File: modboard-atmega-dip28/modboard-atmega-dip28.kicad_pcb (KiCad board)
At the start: 2 copper layers, 57.5 x 52.6 mm, 10 parts, among them J1 modboard-edge-connector, J2 Conn_01x03_Male, U1 ATMEGA328P-PU, Y1 Crystal

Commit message: Added logo
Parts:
- added ATmega-DIP28: LOGO_BRD_REF, qboards_aesthetics:logo_url-3mm, B.Cu at (126.6, 71.3)
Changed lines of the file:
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@@
     (tracks 381)
     (zones 0)
-    (modules 10)
+    (modules 11)
     (nets 28)
   )
   (page A4)
   (layers
-    (0 F.Cu signal)
-    (31 B.Cu signal)
+    (0 F.Cu signal hide)
+    (31 B.Cu signal hide)
     (32 B.Adhes user hide)
     (33 F.Adhes user hide)
@@
   )
   (setup
-    (last_trace_width 0.61)
+    (last_trace_width 0.3048)
     (user_trace_width 0.61)
     (trace_clearance 0.2)
@@
     (add_net "Net-(C2-Pad1)")
     (add_net "Net-(C3-Pad1)")
-    (add_net "Net-(J1-Pad10)")
-    (add_net "Net-(J1-Pad11)")
-    (add_net "Net-(J1-Pad12)")
-    (add_net "Net-(J1-Pad13)")
-    (add_net "Net-(J1-Pad14)")
-    (add_net "Net-(J1-Pad15)")
-    (add_net "Net-(J1-Pad16)")
-    (add_net "Net-(J1-Pad17)")
-    (add_net "Net-(J1-Pad19)")
-    (add_net "Net-(J1-Pad21)")
-    (add_net "Net-(J1-Pad22)")
-    (add_net "Net-(J1-Pad23)")
-    (add_net "Net-(J1-Pad24)")
-    (add_net "Net-(J1-Pad25)")
-    (add_net "Net-(J1-Pad26)")
     (add_net "Net-(J1-Pad27)")
-    (add_net "Net-(J1-Pad28)")
     (add_net "Net-(J1-Pad29)")
-    (add_net "Net-(J1-Pad30)")
     (add_net "Net-(J1-Pad31)")
-    (add_net "Net-(J1-Pad32)")
-    (add_net "Net-(J1-Pad34)")
-    (add_net "Net-(J1-Pad38)")
-    (add_net "Net-(J1-Pad40)")
     (add_net "Net-(J1-Pad43)")
     (add_net "Net-(J1-Pad45)")
@@
     (add_net "Net-(J1-Pad51)")
     (add_net "Net-(J1-Pad53)")
-    (add_net "Net-(J1-Pad56)")
-    (add_net "Net-(J1-Pad57)")
-    (add_net "Net-(J1-Pad62)")
     (add_net "Net-(J1-Pad63)")
-    (add_net "Net-(J1-Pad64)")
     (add_net "Net-(J1-Pad65)")
-    (add_net "Net-(J1-Pad66)")
     (add_net "Net-(J1-Pad67)")
-    (add_net "Net-(J1-Pad68)")
     (add_net "Net-(J1-Pad69)")
     (add_net "Net-(J1-Pad7)")
-    (add_net "Net-(J1-Pad70)")
     (add_net "Net-(J1-Pad71)")
-    (add_net "Net-(J1-Pad72)")
     (add_net "Net-(J1-Pad73)")
-    (add_net "Net-(J1-Pad74)")
-    (add_net "Net-(J1-Pad75)")
-    (add_net "Net-(J1-Pad76)")
-    (add_net "Net-(J1-Pad9)")
-    (add_net "Net-(U1-Pad21)")
     (add_net RESET)
     (add_net RX)
@@
     (add_net VCC)
   )
+  (module qboards_aesthetics:logo_url-3mm (layer B.Cu)
+    (at 126.6 71.3 270)
+    (fp_text reference ATmega-DIP28 (at 2.4384 0.4572 90) (layer B.SilkS)
+      (effects (font (size 0.6 0.6) (thickness 0.1)) (justify left mirror))
+    )
+    (fp_text value LOGO_BRD_REF (at 0 -2.3622 90) (layer B.SilkS) hide
+      (effects (font (size 0.6 0.6) (thickness 0.1)) (justify mirror))
+    )
+    (fp_text user qboards.github.io (at 2.4384 -0.762 90) (layer B.SilkS)
+      (effects (font (size 0.6 0.6) (thickness 0.1)) (justify left mirror))
+    )
+    (fp_poly (pts (xy 0.301751 1.394461) (xy 0.582667 1.316111) (xy 0.844161 1.176542) (xy 1.075553 0.974514)
+      (xy 1.266161 0.708785) (xy 1.303875 0.636973) (xy 1.37773 0.475836) (xy 1.419998 0.342842)
+      (xy 1.439126 0.20029) (xy 1.443566 0.013664) (xy 1.439594 -0.157438) (xy 1.429078 -0.303015)
+      (xy 1.414115 -0.396238) (xy 1.410711 -0.406392) (xy 1.383931 -0.456332) (xy 1.348489 -0.45341)
+      (xy 1.279461 -0.394371) (xy 1.273128 -0.388429) (xy 1.21484 -0.321997) (xy 1.182885 -0.243632)
+      (xy 1.169652 -0.126196) (xy 1.16747 -0.011671) (xy 1.130012 0.29018) (xy 1.02716 0.553497)
+      (xy 0.869991 0.773577) (xy 0.669584 0.945712) (xy 0.437018 1.065199) (xy 0.183372 1.127332)
+      (xy -0.080277 1.127405) (xy -0.342849 1.060714) (xy -0.593266 0.922552) (xy -0.738616 0.797882)
+      (xy -0.922376 0.561969) (xy -1.032169 0.306442) (xy -1.072891 0.042499) (xy -1.049439 -0.218666)
+      (xy -0.966708 -0.465853) (xy -0.829594 -0.687868) (xy -0.642992 -0.873513) (xy -0.411797 -1.011592)
+      (xy -0.140906 -1.090908) (xy 0.09333 -1.104832) (xy 0.248968 -1.102978) (xy 0.34842 -1.116252)
+      (xy 0.419803 -1.151909) (xy 0.478353 -1.204178) (xy 0.587693 -1.313518) (xy 0.422963 -1.359256)
+      (xy 0.178868 -1.397375) (xy -0.090528 -1.392549) (xy -0.338117 -1.345713) (xy -0.343492 -1.344052)
+      (xy -0.660977 -1.204782) (xy -0.925946 -1.007348) (xy -1.132568 -0.76185) (xy -1.275016 -0.47839)
+      (xy -1.347458 -0.167068) (xy -1.344068 0.162016) (xy -1.311358 0.333052) (xy -1.193529 0.648479)
+      (xy -1.020362 0.911375) (xy -0.802536 1.1205) (xy -0.550731 1.274612) (xy -0.275628 1.372471)
+      (xy 0.012092 1.412834) (xy 0.301751 1.394461)) (layer B.SilkS) (width 0.01))
+    (fp_poly (pts (xy 0.229107 0.630267) (xy 0.384132 0.565267) (xy 0.392712 0.559141) (xy 0.571873 0.387566)
+      (xy 0.671563 0.193924) (xy 0.695785 -0.029709) (xy 0.695247 -0.039303) (xy 0.681566 -0.260639)
+      (xy 1.082897 -0.66372) (xy 1.484227 -1.0668) (xy 1.9304 -1.0668) (xy 1.9304 -1.5748)
+      (xy 1.272852 -1.5748) (xy 0.794695 -1.095283) (xy 0.316537 -0.615765) (xy 0.096885 -0.633387)
+      (xy -0.056582 -0.636172) (xy -0.169617 -0.608257) (xy -0.267041 -0.551988) (xy -0.441484 -0.406408)
+      (xy -0.543765 -0.250165) (xy -0.585771 -0.062377) (xy -0.588434 0.0127) (xy -0.563995 0.217089)
+      (xy -0.482479 0.383076) (xy -0.331592 0.533767) (xy -0.296964 0.560417) (xy -0.146721 0.627908)
+      (xy 0.040396 0.651169) (xy 0.229107 0.630267)) (layer B.SilkS) (width 0.01))
+  )
   (module Connector_PinHeader_2.54mm:PinHeader_1x02_P2.54mm_Horizontal (layer F.Cu)

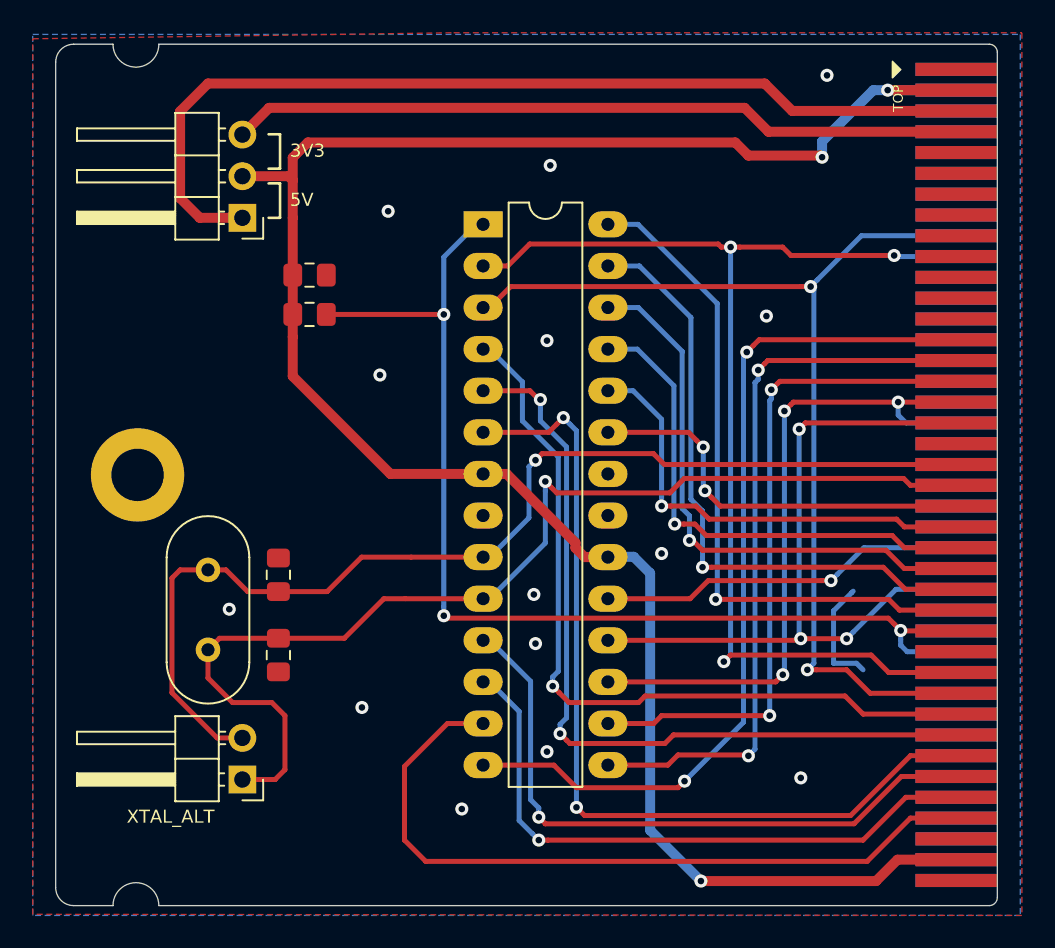
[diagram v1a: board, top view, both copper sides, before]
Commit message: Fixed GND plane
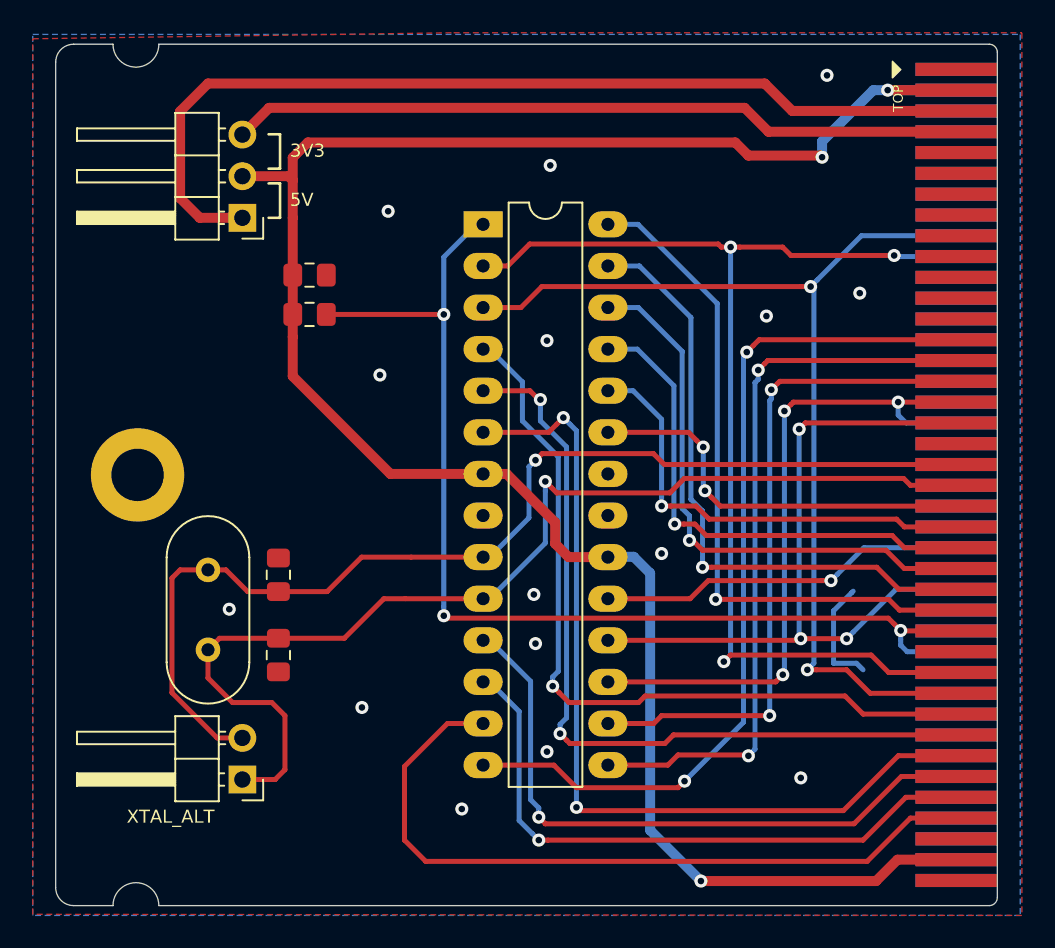
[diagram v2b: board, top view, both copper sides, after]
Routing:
- net VCC: track 127.5 -> 128.1 mm
- net GND: vias 14 -> 15
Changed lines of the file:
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@@
     (thickness 1.6)
     (drawings 23)
-    (tracks 381)
+    (tracks 382)
     (zones 0)
     (modules 11)
@@
   (page A4)
   (layers
-    (0 F.Cu signal hide)
-    (31 B.Cu signal hide)
+    (0 F.Cu signal)
+    (31 B.Cu signal)
     (32 B.Adhes user hide)
     (33 F.Adhes user hide)
-    (34 B.Paste user)
+    (34 B.Paste user hide)
     (35 F.Paste user hide)
-    (36 B.SilkS user)
-    (37 F.SilkS user)
+    (36 B.SilkS user hide)
+    (37 F.SilkS user hide)
     (38 B.Mask user)
     (39 F.Mask user hide)
@@
   (via (at 141.5 86.8) (size 0.8) (drill 0.4) (layers F.Cu B.Cu) (net 1))
   (via (at 140.4 107.1) (size 0.8) (drill 0.4) (layers F.Cu B.Cu) (net 1))
+  (via (at 170.8 81.8) (size 0.8) (drill 0.4) (layers F.Cu B.Cu) (net 1))
   (via (at 168.5 73.5) (size 0.8) (drill 0.4) (layers F.Cu B.Cu) (net 2))
   (segment (start 171.629315 69.405) (end 176.7 69.405) (width 0.61) (layer B.Cu) (net 2))
@@
   (segment (start 135.935 74.66) (end 136.175 74.9) (width 0.61) (layer F.Cu) (net 2))
   (segment (start 133.1 74.66) (end 135.935 74.66) (width 0.61) (layer F.Cu) (net 2))
-  (segment (start 149.24 92.84) (end 147.8 92.84) (width 0.61) (layer F.Cu) (net 2))
-  (segment (start 153.44 97.04) (end 149.24 92.84) (width 0.61) (layer F.Cu) (net 2))
-  (segment (start 153.44 97.36) (end 153.44 97.04) (width 0.61) (layer F.Cu) (net 2))
-  (segment (start 155.42 97.92) (end 154 97.92) (width 0.61) (layer F.Cu) (net 2))
-  (segment (start 154 97.92) (end 153.44 97.36) (width 0.61) (layer F.Cu) (net 2))
   (segment (start 155.82 97.92) (end 155.84 97.9) (width 0.61) (layer B.Cu) (net 2))
   (segment (start 155.42 97.92) (end 155.82 97.92) (width 0.61) (layer B.Cu) (net 2))
@@
   (segment (start 136.175 74.9) (end 136.175 73.525) (width 0.61) (layer F.Cu) (net 2))
   (segment (start 136.175 73.525) (end 137.1 72.6) (width 0.61) (layer F.Cu) (net 2))
+  (segment (start 149.24 92.84) (end 147.8 92.84) (width 0.61) (layer F.Cu) (net 2))
+  (segment (start 152.2 95.8) (end 149.24 92.84) (width 0.61) (layer F.Cu) (net 2))
+  (segment (start 152.2 97.1) (end 152.2 95.8) (width 0.61) (layer F.Cu) (net 2))
+  (segment (start 155.42 97.92) (end 153.02 97.92) (width 0.61) (layer F.Cu) (net 2))
+  (segment (start 153.02 97.92) (end 152.2 97.1) (width 0.61) (layer F.Cu) (net 2))
   (segment (start 147.505 97.625) (end 147.8 97.92) (width 0.3048) (layer F.Cu) (net 3))
   (via (at 151 92) (size 0.8) (drill 0.4) (layers F.Cu B.Cu) (net 3))
@@
   (segment (start 157.28 82.68) (end 159.957212 85.357212) (width 0.3048) (layer B.Cu) (net 17))
   (via (at 161.199022 98.536662) (size 0.8) (drill 0.4) (layers F.Cu B.Cu) (net 18))
-  (segment (start 176.7 99.885) (end 173.585 99.885) (width 0.3048) (layer F.Cu) (net 18))
-  (segment (start 173.585 99.885) (end 172.236662 98.536662) (width 0.3048) (layer F.Cu) (net 18))
-  (segment (start 161.764707 98.536662) (end 161.199022 98.536662) (width 0.3048) (layer F.Cu) (net 18))
-  (segment (start 172.236662 98.536662) (end 161.764707 98.536662) (width 0.3048) (layer F.Cu) (net 18))
   (segment (start 161.199022 97.970977) (end 161.199022 98.536662) (width 0.3048) (layer B.Cu) (net 18))
   (segment (start 161.199022 95.099022) (end 161.199022 97.970977) (width 0.3048) (layer B.Cu) (net 18))
@@
   (segment (start 155.42 80.14) (end 157.34 80.14) (width 0.3048) (layer B.Cu) (net 18))
   (segment (start 157.34 80.14) (end 160.490377 83.290377) (width 0.3048) (layer B.Cu) (net 18))
+  (segment (start 161.764707 98.536662) (end 161.199022 98.536662) (width 0.3048) (layer F.Cu) (net 18))
+  (segment (start 171.836662 98.536662) (end 161.764707 98.536662) (width 0.3048) (layer F.Cu) (net 18))
+  (segment (start 176.7 99.885) (end 173.185 99.885) (width 0.3048) (layer F.Cu) (net 18))
+  (segment (start 173.185 99.885) (end 171.836662 98.536662) (width 0.3048) (layer F.Cu) (net 18))
   (via (at 162 100.5) (size 0.8) (drill 0.4) (layers F.Cu B.Cu) (net 19))
   (segment (start 167.4 100.5) (end 162 100.5) (width 0.3048) (layer F.Cu) (net 19))
@@
   (segment (start 170.905 78.295) (end 168.199999 81.000001) (width 0.3048) (layer B.Cu) (net 21))
   (segment (start 168.199999 81.000001) (end 167.8 81.4) (width 0.3048) (layer B.Cu) (net 21))
-  (segment (start 147.8 82.68) (end 148.2 82.68) (width 0.3048) (layer F.Cu) (net 21))
   (segment (start 167.999999 81.599999) (end 167.8 81.4) (width 0.3048) (layer B.Cu) (net 21))
   (segment (start 167.6 104.8) (end 167.999999 104.400001) (width 0.3048) (layer B.Cu) (net 21))
   (segment (start 167.999999 104.400001) (end 167.999999 81.599999) (width 0.3048) (layer B.Cu) (net 21))
-  (segment (start 167.234315 81.4) (end 167.8 81.4) (width 0.3048) (layer F.Cu) (net 21))
-  (segment (start 149.48 81.4) (end 167.234315 81.4) (width 0.3048) (layer F.Cu) (net 21))
   (segment (start 176.7 78.295) (end 170.905 78.295) (width 0.3048) (layer B.Cu) (net 21))
-  (segment (start 148.2 82.68) (end 149.48 81.4) (width 0.3048) (layer F.Cu) (net 21))
   (segment (start 168.165685 104.8) (end 167.6 104.8) (width 0.3048) (layer F.Cu) (net 21))
   (segment (start 170 104.8) (end 168.165685 104.8) (width 0.3048) (layer F.Cu) (net 21))
   (segment (start 176.7 106.235) (end 171.435 106.235) (width 0.3048) (layer F.Cu) (net 21))
   (segment (start 171.435 106.235) (end 170 104.8) (width 0.3048) (layer F.Cu) (net 21))
+  (segment (start 167.234315 81.4) (end 167.8 81.4) (width 0.3048) (layer F.Cu) (net 21))
+  (segment (start 151.39 81.4) (end 167.234315 81.4) (width 0.3048) (layer F.Cu) (net 21))
+  (segment (start 147.8 82.68) (end 150.11 82.68) (width 0.3048) (layer F.Cu) (net 21))
+  (segment (start 150.11 82.68) (end 151.39 81.4) (width 0.3048) (layer F.Cu) (net 21))
   (via (at 152.04759 105.799999) (size 0.8) (drill 0.4) (layers F.Cu B.Cu) (net 22))
   (segment (start 152.447589 106.199998) (end 152.04759 105.799999) (width 0.3048) (layer F.Cu) (net 22))
@@
   (segment (start 152.5 108.7) (end 152.5 108.134315) (width 0.3048) (layer B.Cu) (net 23))
   (segment (start 152.5 108.134315) (end 152.895189 107.739126) (width 0.3048) (layer B.Cu) (net 23))
-  (segment (start 173.8952 110.045) (end 170.2402 113.7) (width 0.3048) (layer F.Cu) (net 24))
-  (segment (start 176.7 110.045) (end 173.8952 110.045) (width 0.3048) (layer F.Cu) (net 24))
   (via (at 153.5 113.2) (size 0.8) (drill 0.4) (layers F.Cu B.Cu) (net 24))
-  (segment (start 170.2402 113.7) (end 154 113.7) (width 0.3048) (layer F.Cu) (net 24))
-  (segment (start 154 113.7) (end 153.5 113.2) (width 0.3048) (layer F.Cu) (net 24))
   (via (at 152.7 89.4) (size 0.8) (drill 0.4) (layers F.Cu B.Cu) (net 24))
   (segment (start 152.300001 89.799999) (end 152.7 89.4) (width 0.3048) (layer F.Cu) (net 24))
@@
   (segment (start 153.099999 89.799999) (end 152.7 89.4) (width 0.3048) (layer B.Cu) (net 24))
   (segment (start 153.5 113.2) (end 153.5 90.2) (width 0.3048) (layer B.Cu) (net 24))
+  (segment (start 153.7 113.4) (end 153.5 113.2) (width 0.3048) (layer F.Cu) (net 24))
+  (segment (start 169.8 113.4) (end 153.7 113.4) (width 0.3048) (layer F.Cu) (net 24))
+  (segment (start 176.7 110.045) (end 173.155 110.045) (width 0.3048) (layer F.Cu) (net 24))
+  (segment (start 173.155 110.045) (end 169.8 113.4) (width 0.3048) (layer F.Cu) (net 24))
   (segment (start 151.60481 114.20481) (end 151.599999 114.199999) (width 0.3048) (layer F.Cu) (net 25))
   (segment (start 151.599999 114.199999) (end 151.2 113.8) (width 0.3048) (layer F.Cu) (net 25))

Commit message: Added rev number, added sheet data
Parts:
- ATmega-DIP28 | Rev 1.0: renamed from ATmega-DIP28
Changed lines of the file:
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@@
   )
   (page A4)
+  (title_block
+    (title ATmega-Dip28)
+    (rev 1.0)
+    (company QBoards)
+  )
   (layers
     (0 F.Cu signal)
@@
     (34 B.Paste user hide)
     (35 F.Paste user hide)
-    (36 B.SilkS user hide)
+    (36 B.SilkS user)
     (37 F.SilkS user hide)
-    (38 B.Mask user)
+    (38 B.Mask user hide)
     (39 F.Mask user hide)
     (40 Dwgs.User user hide)
@@
       (outputformat 1)
       (mirror false)
-      (drillshape 1)
+      (drillshape 0)
       (scaleselection 1)
-      (outputdirectory ""))
+      (outputdirectory "gerbers/"))
   )
   (net 0 "")
@@
   (module qboards_aesthetics:logo_url-3mm (layer B.Cu)
     (at 126.6 71.3 270)
-    (fp_text reference ATmega-DIP28 (at 2.4384 0.4572 90) (layer B.SilkS)
+    (fp_text reference "ATmega-DIP28 | Rev 1.0" (at 2.4384 0.4572 90) (layer B.SilkS)
       (effects (font (size 0.6 0.6) (thickness 0.1)) (justify left mirror))
     )

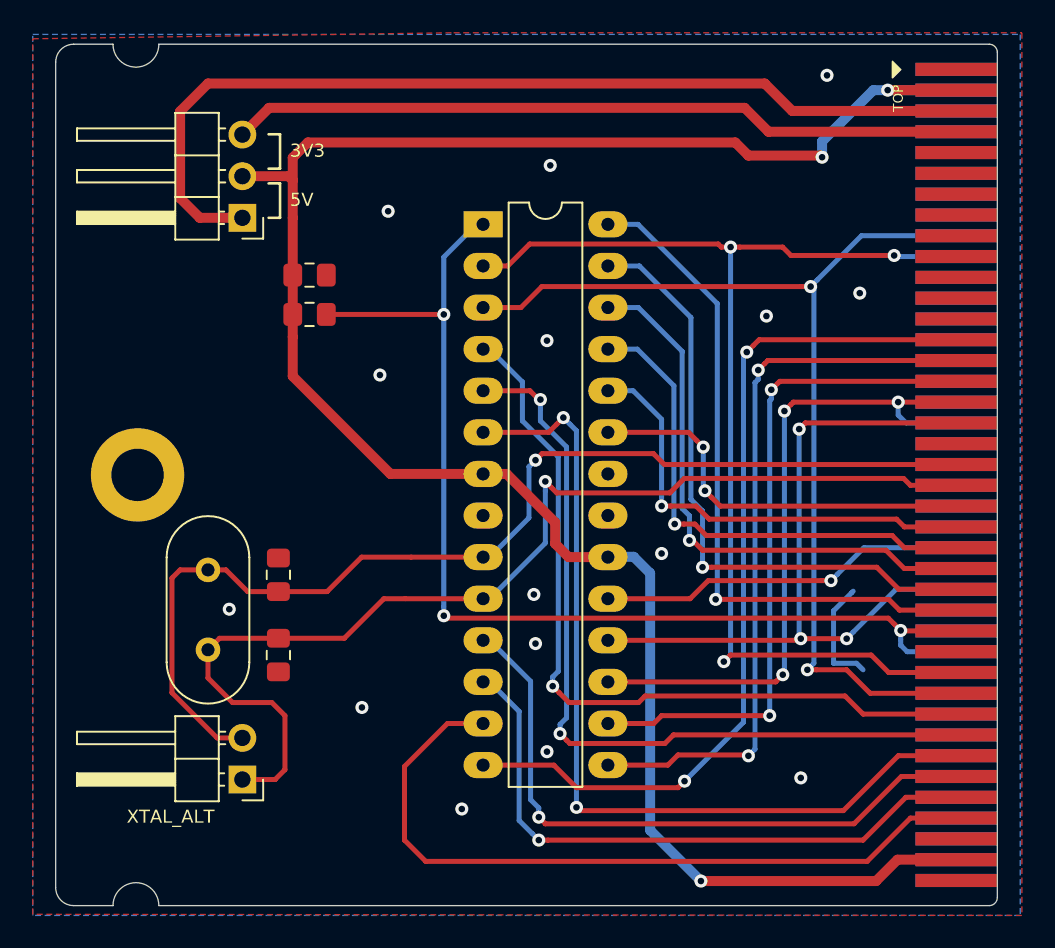
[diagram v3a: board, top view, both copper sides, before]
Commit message: Updated board size, connector and reference text
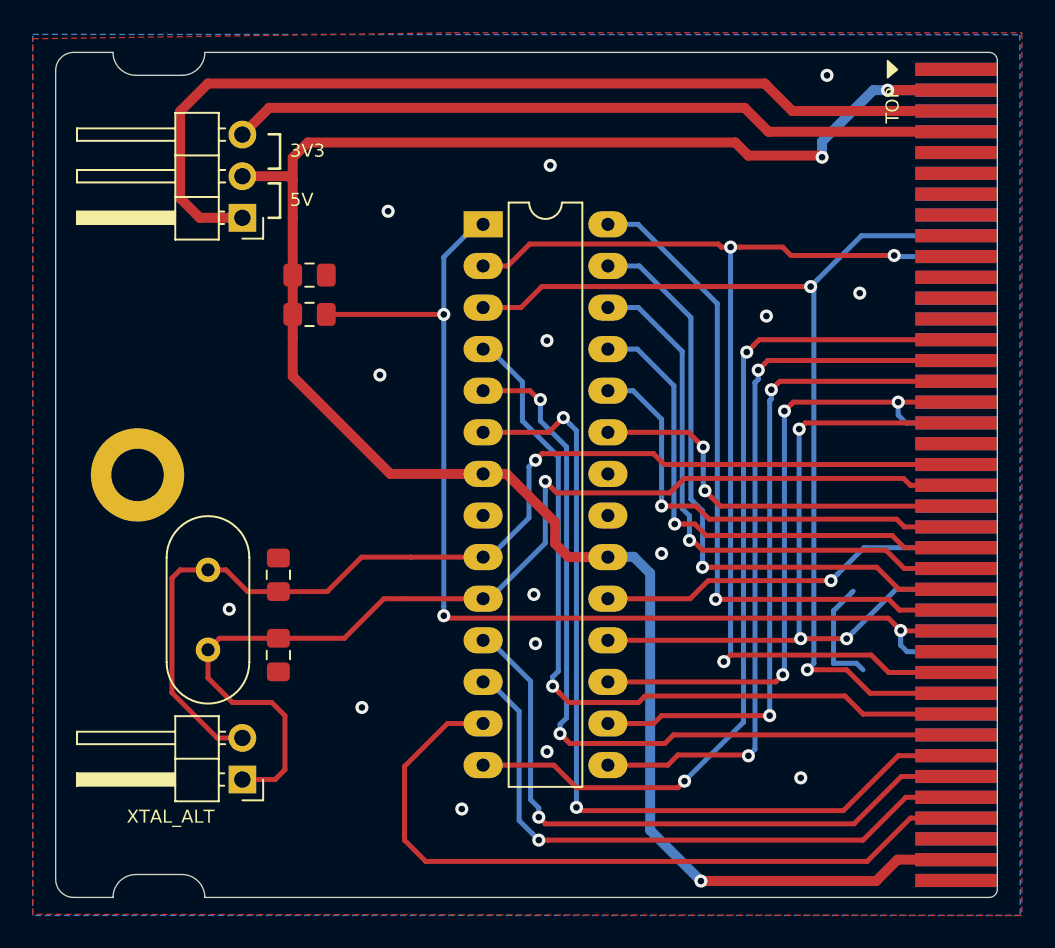
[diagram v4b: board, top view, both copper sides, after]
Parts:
- removed ATmega-DIP28 | Rev 1.0: LOGO_BRD_REF, qboards_aesthetics:logo_url-3mm
- added ATmega-DIP28: LOGO_BRD_REF, qboards_aesthetics:logo_url-5mm, B.Cu at (126.4, 71.8)
- moved J1 0.50 mm to (176.7, 67.1)
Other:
- board size 57.5 x 52.6 mm -> 57.5 x 51.6 mm
- board text added: "Rev 1.1"
